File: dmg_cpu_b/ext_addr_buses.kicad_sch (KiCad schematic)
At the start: 128 parts

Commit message: CH1 Regs page completed.
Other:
- company: (none) -> CC-BY-SA-4.0 Régis Galland & Michael Singer -- Derived work from Furrtek
- title: (none) -> DMG CPU B
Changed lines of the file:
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@@
 (kicad_sch (version 20211123) (generator eeschema)
   (paper "A3")
+  (title_block
+    (title "DMG CPU B")
+    (date "2022-03-12")
+    (rev "0")
+    (company "CC-BY-SA-4.0 Régis Galland & Michael Singer -- Derived work from Furrtek")
+    (comment 1 "https://github.com/msinger/dmg-schematics")
+  )
   (junction (at 180.34 85.09) (diameter 0) (color 0 0 0 0)
   )

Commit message: fixes made following review
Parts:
- AJOV, AKAN, ANAR, AZUV, BYNA, BYNE, BYXE, KEJO, LEFY, LOFA, LORA, LYNA, MAPU, NEFE, RALA, SYZU: value TRI_INV_IF0 -> TRI_BUF_IF0; symbol DMG_CPU_Cells:TRI_INV_IF0 -> DMG_CPU_Cells:TRI_BUF_IF0
- renumbered AMET to MANO
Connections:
- net EXT_PIN_DIR is gone; now on net ~{EXT_ADDR_EN}: LABE.2, LEPY.2, LUCE.2, MUNE.2, MYNY.2, PUHE.2, ROXU.2, TOVA.2
- net A0: now also KEJO.4; no longer KEJO.3
- net A1: now also BYXE.4; no longer BYXE.3
- net A10: now also RALA.4; no longer RALA.3
- net A11: now also LORA.4; no longer LORA.3
- net A12: now also LYNA.4; no longer LYNA.3
- net A13: now also LEFY.4; no longer LEFY.3
- net A14: now also NEFE.4; no longer NEFE.3
- net A15: now also SYZU.4; no longer SYZU.3
- net A2: now also AKAN.4; no longer AKAN.3
- net A3: now also ANAR.4; no longer ANAR.3
- net A4: now also AZUV.4; no longer AZUV.3
- net A5: now also AJOV.4; no longer AJOV.3
- net A6: now also BYNE.4; no longer BYNE.3
- net A7: now also BYNA.4; no longer BYNA.3
- net A8: now also LOFA.4; no longer LOFA.3
- net A9: now also MAPU.4; no longer MAPU.3
- net DMA_A0: no longer APOK.2, ATOL.2, MALE.2, MASU.2, MOJY.2, MUCE.2, PAMY.2
- net ~{EXT_ADDR_EN}: now also AJOV.2 (~{ENA}), AKAN.2 (~{ENA}), ANAR.2 (~{ENA}), AZUV.2 (~{ENA}), BYNA.2 (~{ENA}), BYNE.2 (~{ENA}), BYXE.2 (~{ENA}), KEJO.2 (~{ENA}), LEFY.2 (~{ENA}), LOFA.2 (~{ENA}), LORA.2 (~{ENA}), LYNA.2 (~{ENA}), MAPU.2 (~{ENA}), NEFE.2 (~{ENA}), RALA.2 (~{ENA}); no longer AJOV.1 (~{ENA}), AKAN.1 (~{ENA}), ANAR.1 (~{ENA}), AZUV.1 (~{ENA}), BYNA.1 (~{ENA}), BYNE.1 (~{ENA}), BYXE.1 (~{ENA}), KEJO.1 (~{ENA}), LEFY.1 (~{ENA}), LOFA.1 (~{ENA}), LORA.1 (~{ENA}), LYNA.1 (~{ENA}), MAPU.1 (~{ENA}), NEFE.1 (~{ENA}), RALA.1 (~{ENA}), RYCA.2, SUZE.2, SYZU.1 (~{ENA})
- net at CYGU.2: now also BYNE.1 (IN), BYNE.3 (IN); no longer BYNE.2
- net at ABUP.2: now also AJOV.1 (IN), AJOV.3 (IN); no longer AJOV.2
- net at NENA.2: now also MAPU.1 (IN), MAPU.3 (IN); no longer MAPU.2
- net at KOVA.2: now also KEJO.1 (IN), KEJO.3 (IN); no longer KEJO.2
- net at PEVO.2: now also NEFE.1 (IN), NEFE.3 (IN); no longer NEFE.2
- net at MUJY.2: now also LOFA.1 (IN), LOFA.3 (IN); no longer LOFA.2
- net at RAZA.2: now also SYZU.1 (IN), SYZU.3 (IN); no longer SYZU.2
- net at MADY.2: now also LORA.1 (IN), LORA.3 (IN); no longer LORA.2
- net at BASE.2: now also ANAR.1 (IN), ANAR.3 (IN); no longer ANAR.2
- net at COGO.2: now also BYNA.1 (IN), BYNA.3 (IN); no longer BYNA.2
- net at AFEC.2: now also AZUV.1 (IN), AZUV.3 (IN); no longer AZUV.2
- net at SURA.2: now also RALA.1 (IN), RALA.3 (IN); no longer RALA.2
- net at LAHE.2: now also LYNA.1 (IN), LYNA.3 (IN); no longer LYNA.2
- net at LURA.2: now also LEFY.1 (IN), LEFY.3 (IN); no longer LEFY.2
- net at BUXU.2: now also AKAN.1 (IN), AKAN.3 (IN); no longer AKAN.2
- net at CAMU.2: now also BYXE.1 (IN), BYXE.3 (IN); no longer BYXE.2
- new net: RYCA.2, SUZE.2, SYZU.2 (~{ENA})
- new net DMA_A1: ATOL.2
- new net DMA_A10: PAMY.2
- new net DMA_A11: MALE.2
- new net DMA_A12: MOJY.2
- new net DMA_A13: MUCE.2
- new net DMA_A2: APOK.2
- new net DMA_A9: MASU.2
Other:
- moved on the sheet: A10, A11, A12, A13, A14, A15, A8, A9, LABE, LAHE, LASY, LEPY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

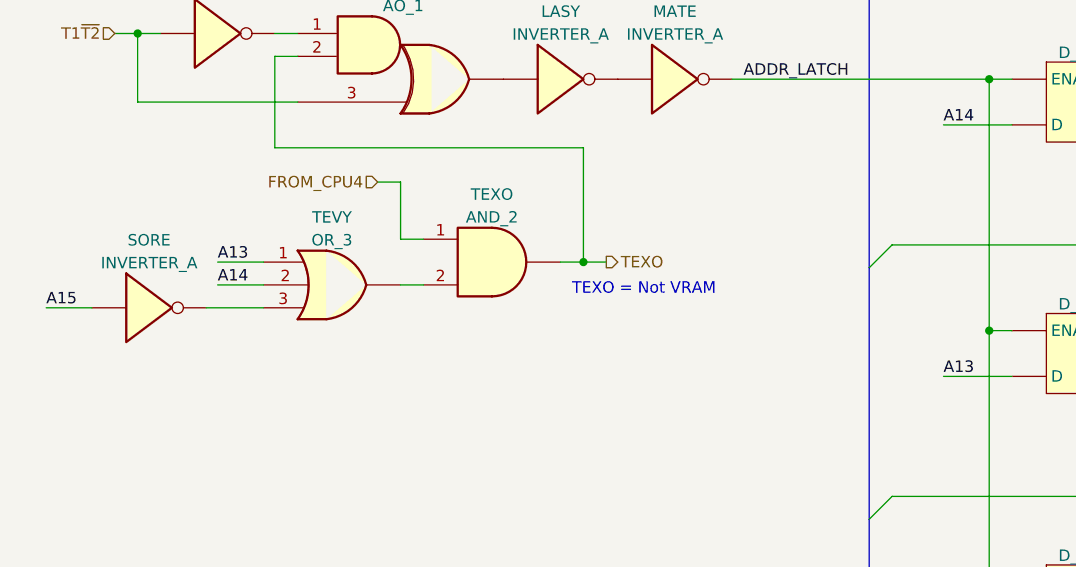
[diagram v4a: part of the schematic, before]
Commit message: VRAM interface sheet added but various edits in existing sheets. Notable merge of RESET, CLOCKS and FF04 DIV sheets
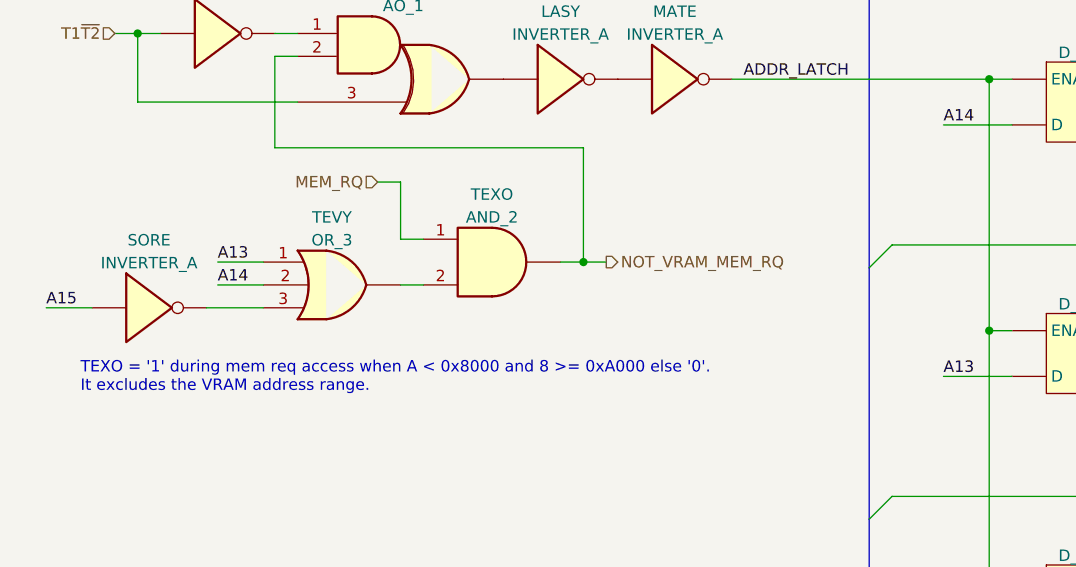
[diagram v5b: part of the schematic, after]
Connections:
- net FROM_CPU4 renamed MEM_RQ
- net TEXO renamed NOT_VRAM_MEM_RQ
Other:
- note added: "TEXO = '1' during mem req access when A < 0x8000 and 8 >= 0xA000 else '0'. It excludes the VRAM address range."
- note removed: "TEXO = Not VRAM"
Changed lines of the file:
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@@
   (title_block
     (title "DMG CPU B")
-    (date "2022-03-12")
+    (date "2022-05-02")
     (rev "0")
     (company "CC-BY-SA-4.0 Régis Galland & Michael Singer -- Derived work from Furrtek")
@@
     (stroke (width 0) (type default) (color 0 0 0 0))
   )
+  (wire (pts (xy 59.055 109.855) (xy 61.595 109.855))
+    (stroke (width 0) (type default) (color 0 0 0 0))
+  )
   (wire (pts (xy 244.475 261.62) (xy 244.475 259.08))
     (stroke (width 0) (type default) (color 0 0 0 0))
@@
     (stroke (width 0) (type default) (color 0 0 0 0))
   )
-  (wire (pts (xy 61.595 109.855) (xy 59.055 109.855))
-    (stroke (width 0) (type default) (color 0 0 0 0))
-  )
   (wire (pts (xy 314.325 42.545) (xy 321.945 42.545))
     (stroke (width 0) (type default) (color 0 0 0 0))
@@
     (stroke (width 0) (type default) (color 0 0 0 0))
   )
-  (text "TEXO = Not VRAM\n" (at 80.645 122.555 0)
+  (text "TEXO = '1' during mem req access when A < 0x8000 and 8 >= 0xA000 else '0'.\nIt excludes the VRAM address range."
+    (at 26.035 133.35 0)
     (effects (font (size 1.27 1.27)) (justify left bottom))
   )
@@
     (effects (font (size 1.27 1.27)) (justify right))
   )
-  (hierarchical_label "TEXO" (shape output) (at 84.455 118.745 0)
+  (hierarchical_label "NOT_VRAM_MEM_RQ" (shape output) (at 84.455 118.745 0)
     (effects (font (size 1.27 1.27)) (justify left))
   )
@@
     (effects (font (size 1.27 1.27)) (justify right))
   )
-  (hierarchical_label "FROM_CPU4" (shape input) (at 59.055 109.855 180)
+  (hierarchical_label "MEM_RQ" (shape input) (at 59.055 109.855 180)
     (effects (font (size 1.27 1.27)) (justify right))
   )

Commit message: Minor tweaks to help with clarity.
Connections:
- net T1~{T2}: now also AJAV.1, BAJO.1, BEVO.1, BOLA.1, COLO.1, COTU.1, CYKA.1, KOTY.1, LEVA.1, LOSO.1, LYNY.1, MEGO.1, MENY.1, PAHY.1, RORE.1, RULO.2, RYCA.1, TOVA.1; no longer LOXO.3, MULE.1
- net ~{T1}T2: now also LOXO.3, MULE.1; no longer AJAV.1, BAJO.1, BEVO.1, BOLA.1, COLO.1, COTU.1, CYKA.1, KOTY.1, LEVA.1, LOSO.1, LYNY.1, MEGO.1, MENY.1, PAHY.1, RORE.1, RULO.2, RYCA.1, TOVA.1
- net ~{EXT_A15_EN}: now reaches RYCA.2, SUZE.2, SYZU.2 (~{ENA})
- net AXXX-FXXX: now reaches TOZA.1, TYNU.4
- net ABUZ renamed RAM_CS_EN
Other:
- note added: "TEXO = '1' during mem req access when A < 0x8000 or A >= 0xA000 else '0'. It excludes the VRAM address range. A0-14 are latched and presented to external pins when driven by CPU"
- note added: "TYNU = '1' when A >= 0xA000 else '0'. TOZA = '1' when A >= 0xA000 and < 0xFE00; RAM space ~{RAM_CS} can only go low in RAM space when driven by CPU"
- note removed: "TEXO = '1' during mem req access when A < 0x8000 and 8 >= 0xA000 else '0'. It excludes the VRAM address range."
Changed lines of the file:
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@@
     (stroke (width 0) (type default) (color 0 0 0 0))
   )
-  (text "TEXO = '1' during mem req access when A < 0x8000 and 8 >= 0xA000 else '0'.\nIt excludes the VRAM address range."
-    (at 26.035 133.35 0)
+  (text "TEXO = '1' during mem req access when A < 0x8000 or A >= 0xA000 else '0'.\nIt excludes the VRAM address range.\nA0-14 are latched and presented to external pins when driven by CPU "
+    (at 19.05 136.525 0)
+    (effects (font (size 1.27 1.27)) (justify left bottom))
+  )
+  (text "TYNU = '1' when A >= 0xA000 else '0'.\nTOZA = '1' when A >= 0xA000 and < 0xFE00; RAM space\n~{RAM_CS} can only go low in RAM space when driven by CPU"
+    (at 41.91 23.495 0)
     (effects (font (size 1.27 1.27)) (justify left bottom))
   )
@@
     (effects (font (size 1.27 1.27)) (justify left bottom))
   )
+  (label "~{EXT_A15_EN}" (at 188.595 21.59 0)
+    (effects (font (size 1.27 1.27)) (justify left bottom))
+  )
   (label "A10" (at 121.92 215.265 0)
     (effects (font (size 1.27 1.27)) (justify left bottom))
@@
     (effects (font (size 1.27 1.27)) (justify left bottom))
   )
+  (label "AXXX-FXXX" (at 110.49 28.575 0)
+    (effects (font (size 1.27 1.27)) (justify left bottom))
+  )
   (label "A9" (at 258.445 238.76 180)
     (effects (font (size 1.27 1.27)) (justify right bottom))
@@
     (effects (font (size 1.27 1.27)) (justify right bottom))
   )
-  (label "~{T1}T2" (at 164.465 36.83 0)
+  (label "T1~{T2}" (at 164.465 36.83 0)
     (effects (font (size 1.27 1.27)) (justify left bottom))
   )
@@
     (effects (font (size 1.27 1.27)) (justify left bottom))
   )
-  (label "~{T1}T2" (at 307.975 23.495 0)
+  (label "T1~{T2}" (at 307.975 23.495 0)
     (effects (font (size 1.27 1.27)) (justify left bottom))
   )
@@
     (effects (font (size 1.27 1.27)) (justify left bottom))
   )
-  (label "~{T1}T2" (at 128.905 67.31 0)
+  (label "T1~{T2}" (at 128.905 67.31 0)
     (effects (font (size 1.27 1.27)) (justify left bottom))
   )
@@
     (effects (font (size 1.27 1.27)) (justify right))
   )
-  (hierarchical_label "T1~{T2}" (shape input) (at 29.845 93.345 180)
+  (hierarchical_label "~{T1}T2" (shape input) (at 29.845 93.345 180)
     (effects (font (size 1.27 1.27)) (justify right))
   )
@@
     (effects (font (size 1.27 1.27)) (justify left))
   )
-  (hierarchical_label "~{T1}T2" (shape input) (at 128.905 67.31 180)
+  (hierarchical_label "T1~{T2}" (shape input) (at 128.905 67.31 180)
     (effects (font (size 1.27 1.27)) (justify right))
   )
@@
     (effects (font (size 1.27 1.27)) (justify right))
   )
-  (hierarchical_label "ABUZ" (shape input) (at 126.365 31.115 180)
-    (effects (font (size 1.27 1.27)) (justify right))
-  )
+  (hierarchical_label "RAM_CS_EN" (shape input) (at 126.365 31.115 180)
+    (effects (font (size 1.27 1.27)) (justify right))
+  )

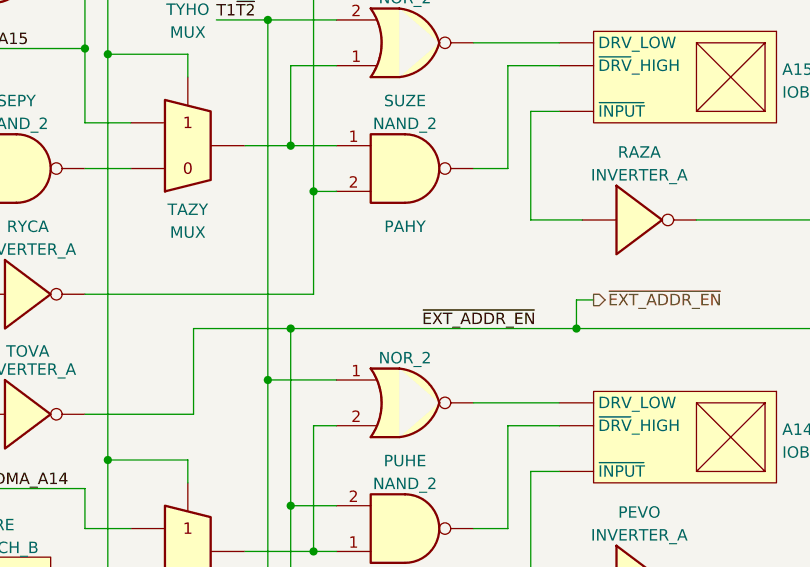
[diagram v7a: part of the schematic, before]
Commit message: Quite a few fixes from review.
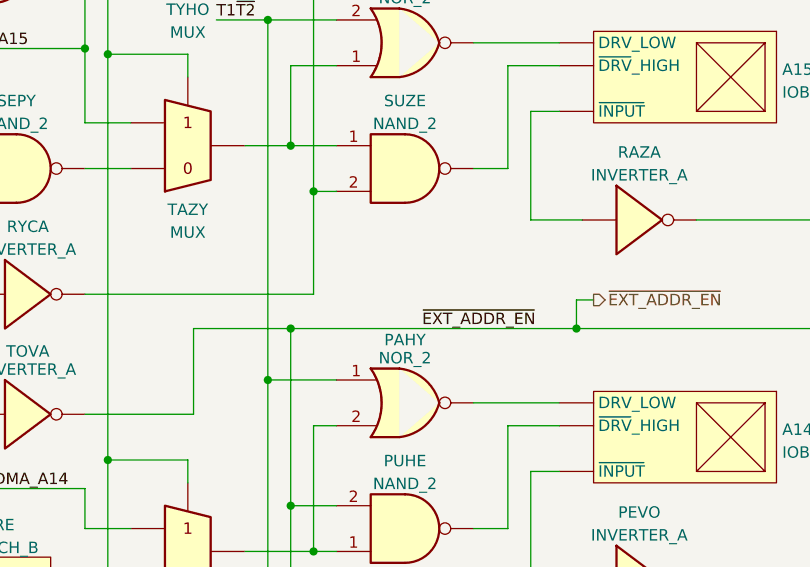
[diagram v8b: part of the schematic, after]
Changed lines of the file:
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@@
   (symbol (lib_id "DMG_CPU_Cells:NOR_2") (at 185.42 79.375 0) (unit 1)
     (in_bom yes) (on_board yes)
-    (property "Reference" "PAHY" (id 0) (at 185.4198 59.8002 0))
+    (property "Reference" "PAHY" (id 0) (at 185.42 72.39 0))
     (property "Value" "NOR_2" (id 1) (at 185.4198 74.4021 0))
     (property "Footprint" "" (id 2) (at 185.166 79.375 0)
